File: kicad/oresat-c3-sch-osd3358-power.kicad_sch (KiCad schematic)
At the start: 52 parts, among them Q6 MMBT2907, U1 OSD3358-512M-BSM, U10 SN74LVC1G07DCK, U13 RCLAMP0504FB, U14 TLVH431

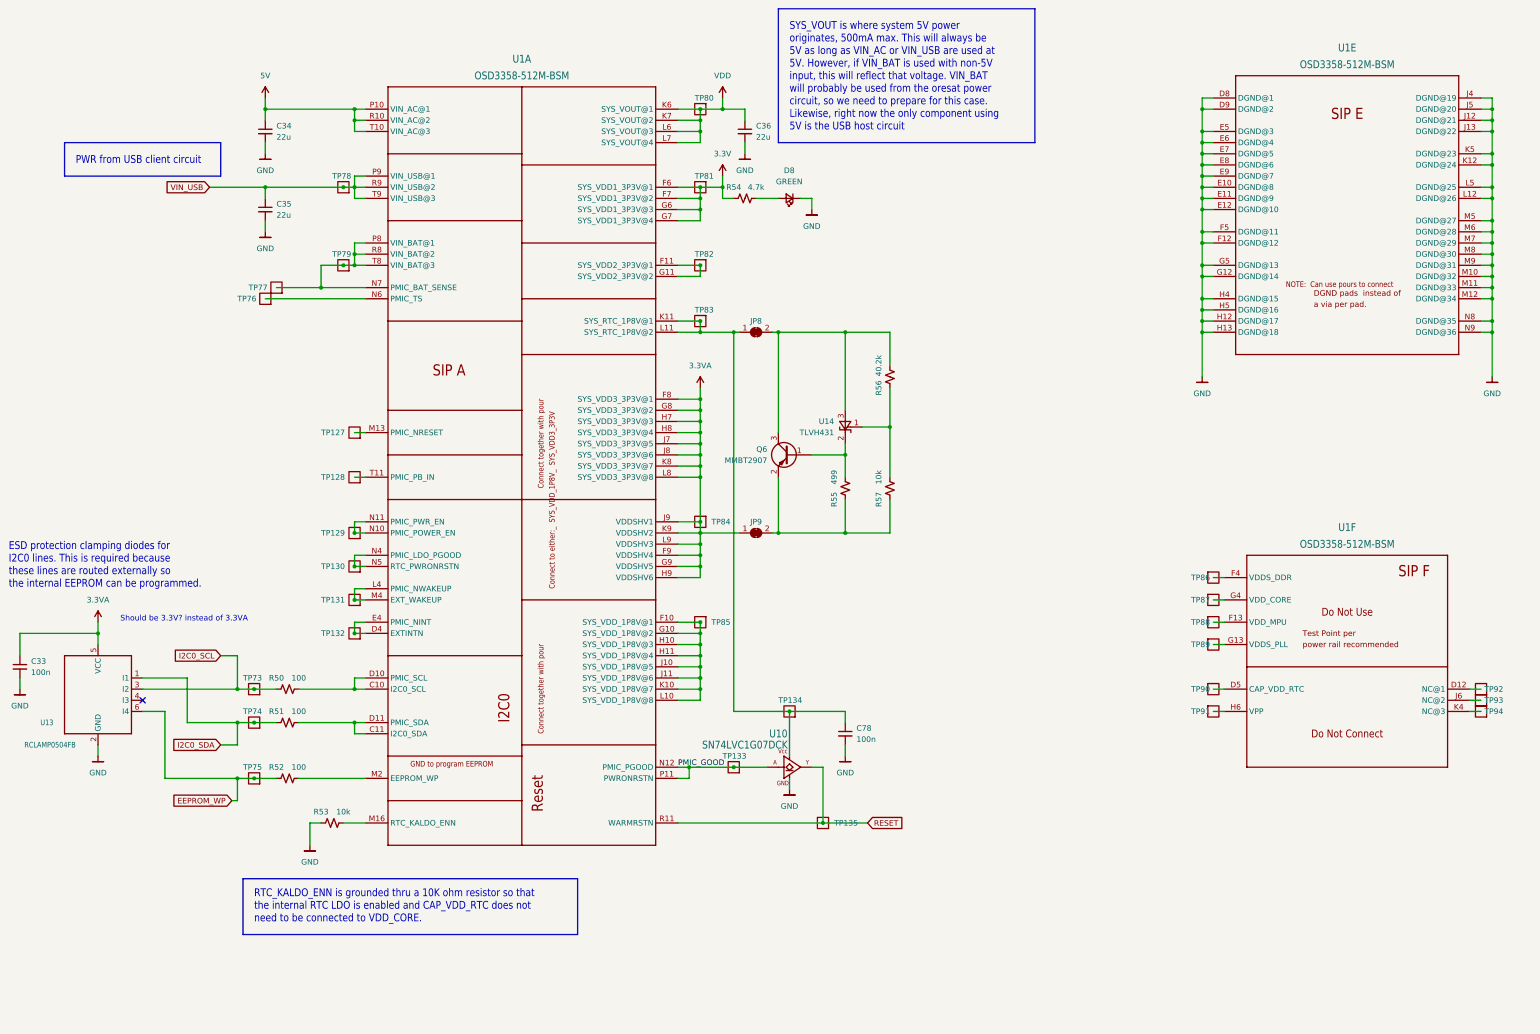
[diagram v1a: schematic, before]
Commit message: C3 v6 schematic now 80% done. OSD2258 IC has been gone over with a fine tooth comb and simplified as much as possible. OSD3358 pinout compared to RED board and PocketBeagle. What's left: lots of little issues, footprints, and then L band and UHF radio schematics need to be fixed.
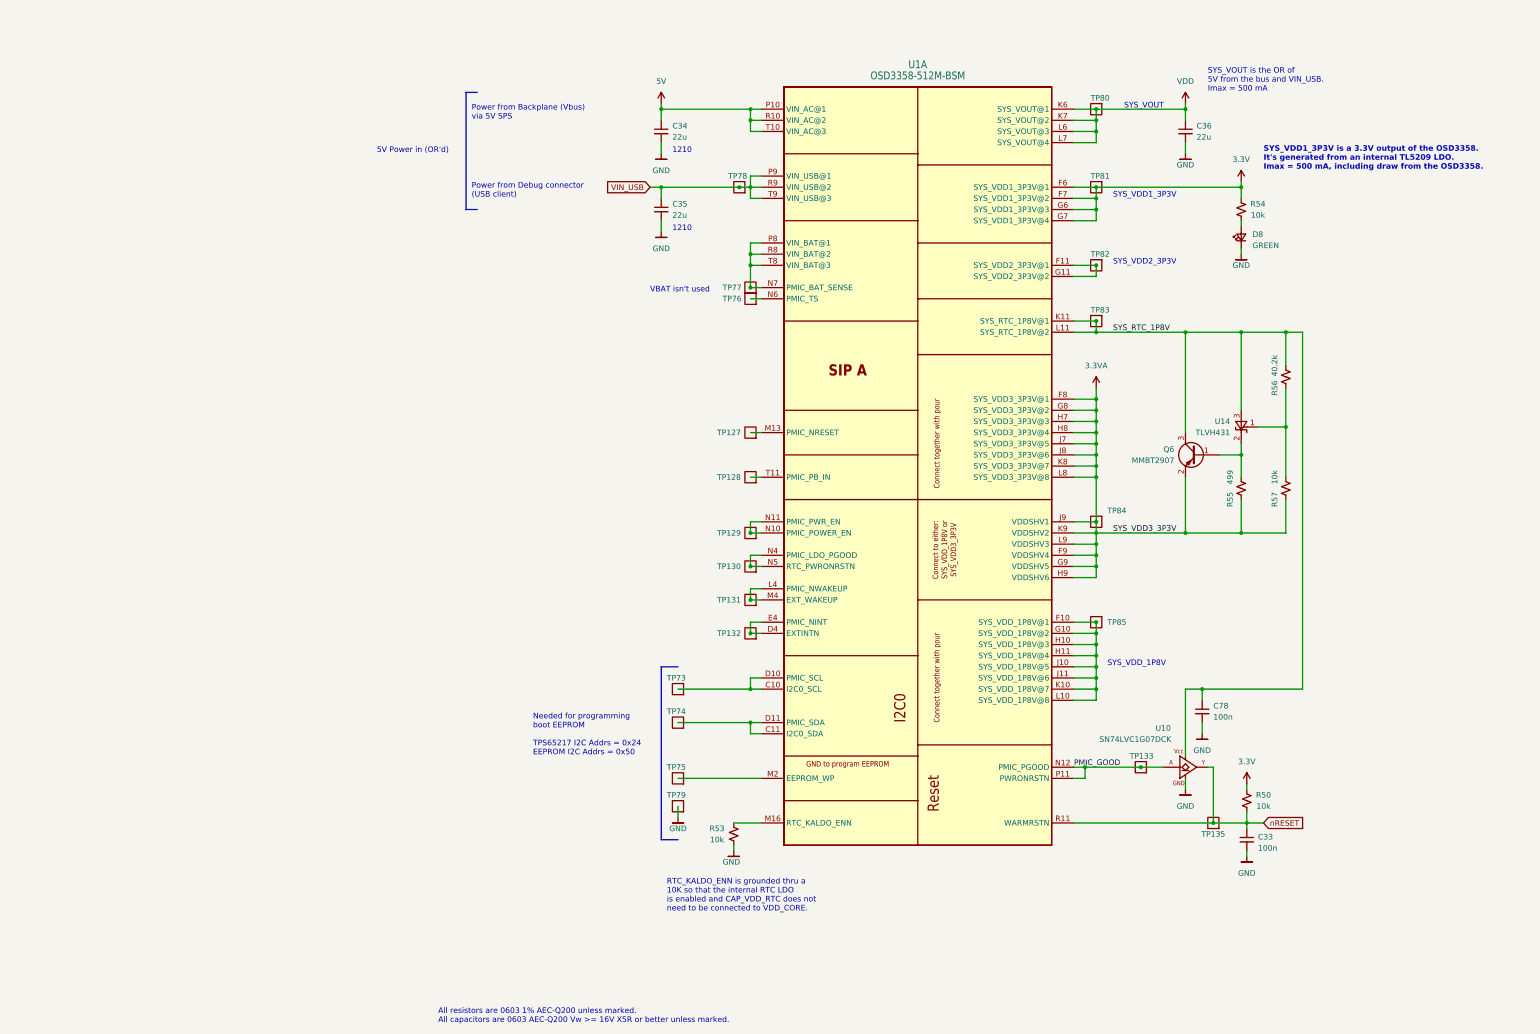
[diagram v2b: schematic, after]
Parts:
- removed JP8, JP9: SolderJumper_2_Bridged, oresat-footprints:SMT-JUMPER_2_NC_TRACE_SILK, symbol Jumper:SolderJumper_2_Bridged
- removed R51, R52: 100, Resistor_SMD:R_0603_1608Metric, symbol Device:R_Small_US
- removed TP134, TP86, TP87, TP88, TP89, TP90, TP91, TP92, TP93, TP94: Test-Point, OreSat-TestPoint:PAD.03X.04, symbol OreSat-TestPoint:Test-Point
- removed unit 6 of U1
- removed unit 5 of U1
- removed U13: RCLAMP0504FB, Package_TO_SOT_SMD:SOT-363_SC-70-6, symbol U-Semtech-RCLAMP0504FB-tvs-diodes:RCLAMP0504FB
- R50: value 100 -> 10k
- R54: value 4.7k -> 10k
- U1: symbol U-OSD3358-512M-BSM:OSD3358-512M-BSM -> oresat-ics:OSD3358-512M-BSM
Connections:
- net EEPROM_WP is gone; now on an unnamed net: TP75.1
- net I2C0_SDA is gone; now on an unnamed net: TP74.1
- net RESET is gone; now on net nRESET: TP135.1, U1.R11 (WARMRSTN), U10.4 (Y)
- net 3.3V: now also R50.2
- net 3.3VA: now also Q6.2 (E), R55.1, R57.1; no longer C33.1
- net GND: now also TP79.1
- net SYS_RTC_1P8V: now reaches C78.1, TP83.1, U1.K11 (SYS_RTC_1P8V@1), U1.L11 (SYS_RTC_1P8V@2), U10.5 (VCC)
- net SYS_RTC_1P8V: now also Q6.3 (C), R56.2, U14.3 (A)
- net at TP77.1, U1.N7 (PMIC_BAT_SENSE), U1.P8 (VIN_BAT@1)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: no longer TP79.1
- net at U1.C10 (I2C0_SCL), U1.D10 (PMIC_SCL): now also TP73.1; no longer R50.2
- net I2C0_SCL renamed nRESET
- net nRESET: now also C33.1; no longer TP73.1
- no-connect marks 1 -> 0
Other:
- note added: "1210"
- note added: "5V Power in (OR'd)"
- note added: "All resistors are 0603 1% AEC-Q200 unless marked. All capacitors are 0603 AEC-Q200 Vw >= 16V X5R or better unless marked."
- note added: "Needed for programming boot EEPROM TPS65217 I2C Addrs = 0x24 EEPROM I2C Addrs = 0x50"
- note added: "Power from Backplane (Vbus) via 5V SPS"
- note added: "Power from Debug connector (USB client)"
- note added: "RTC_KALDO_ENN is grounded thru a 10K so that the internal RTC LDO is enabled and CAP_VDD_RTC does not need to be connected to VDD_CORE."
- note added: "SYS_VDD1_3P3V"
- note added: "SYS_VDD1_3P3V is a 3.3V output of the OSD3358. It's generated from an internal TL5209 LDO. Imax = 500 mA, including draw from the OSD3358."
- note added: "SYS_VDD2_3P3V"
- note added: "SYS_VDD_1P8V"
- note added: "SYS_VOUT"
- note added: "SYS_VOUT is the OR of 5V from the bus and VIN_USB. Imax = 500 mA"
- note added: "VBAT isn't used"
- note removed: "ESD protection clamping diodes for I2C0 lines. This is required because these lines are routed externally so the internal EEPROM can be programmed."
- note removed: "PWR from USB client circuit"
- note removed: "RTC_KALDO_ENN is grounded thru a 10K ohm resistor so that the internal RTC LDO is enabled and CAP_VDD_RTC does not need to be connected to VDD_CORE."
- note removed: "SYS_VOUT is where system 5V power originates, 500mA max. This will always be 5V as long as VIN_AC or VIN_USB are used at 5V. However, if VIN_BAT is used with non-5V input, this will reflect that voltage. VIN_BAT will probably be used from the oresat power circuit, so we need to prepare for this case. Likewise, right now the only component using 5V is the USB host circuit"
- note removed: "Should be 3.3V? instead of 3.3VA"
- title: (none) -> OreSat C3: OSD3358: SIP A
- moved on the sheet: C34, C35, C36, C78, D8, Q6, R53, R54, R55, R56, R57, TP127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

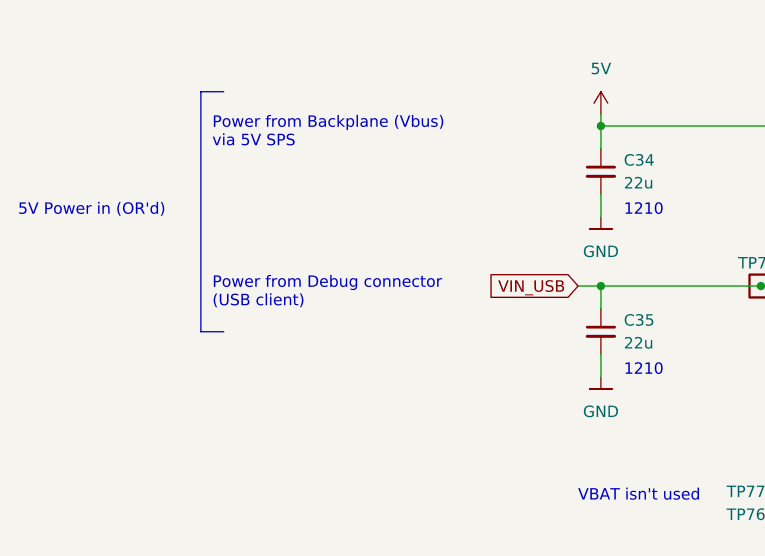
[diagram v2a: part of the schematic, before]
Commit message: Finished UHF radio schematic. Added sheet numbers to external labels. Still to do: L band radio, hooking up GPIO to the OSD3358, and test points.
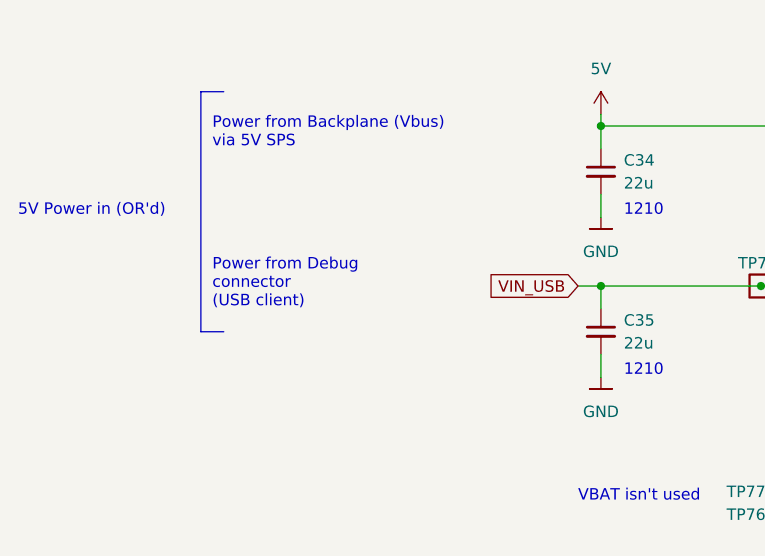
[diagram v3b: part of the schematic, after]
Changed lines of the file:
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@@
     (effects (font (size 1.27 1.27) (thickness 0.254) bold) (justify left bottom))
   )
-  (text "Power from Debug connector\n(USB client)" (at 123.19 73.66 0)
+  (text "Power from Debug \nconnector\n(USB client)" (at 123.19 73.66 0)
     (effects (font (size 1.27 1.27)) (justify left bottom))
   )
@@
     (effects (font (size 1.27 1.27)) (justify right))
     (property "Intersheetrefs" "${INTERSHEET_REFS}" (at 153.6155 71.0406 0)
-      (effects (font (size 1.27 1.27)) (justify right) hide)
+      (effects (font (size 1.27 1.27)) (justify right))
     )
   )
@@
     (effects (font (size 1.27 1.27)) (justify left))
     (property "Intersheetrefs" "${INTERSHEET_REFS}" (at 313.3299 215.9 0)
-      (effects (font (size 1.27 1.27)) (justify left) hide)
+      (effects (font (size 1.27 1.27)) (justify left))
     )
   )

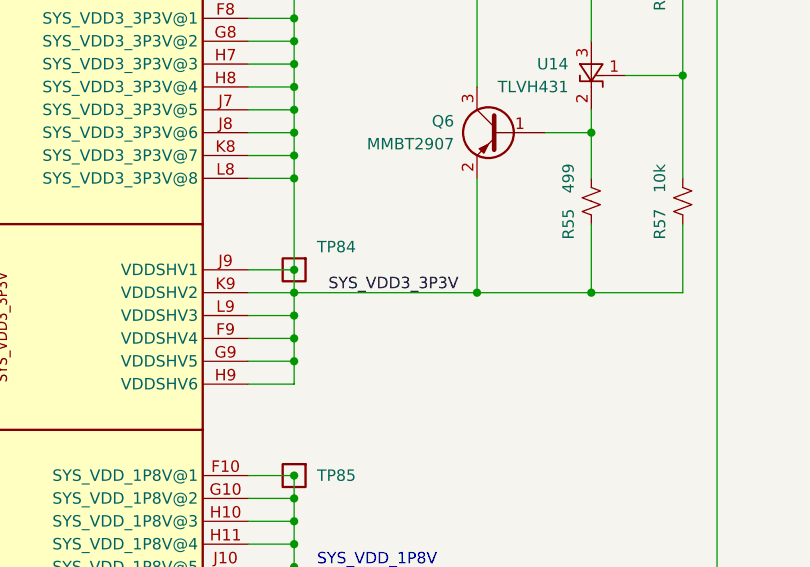
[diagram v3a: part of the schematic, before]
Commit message: First round of ERC fixes.
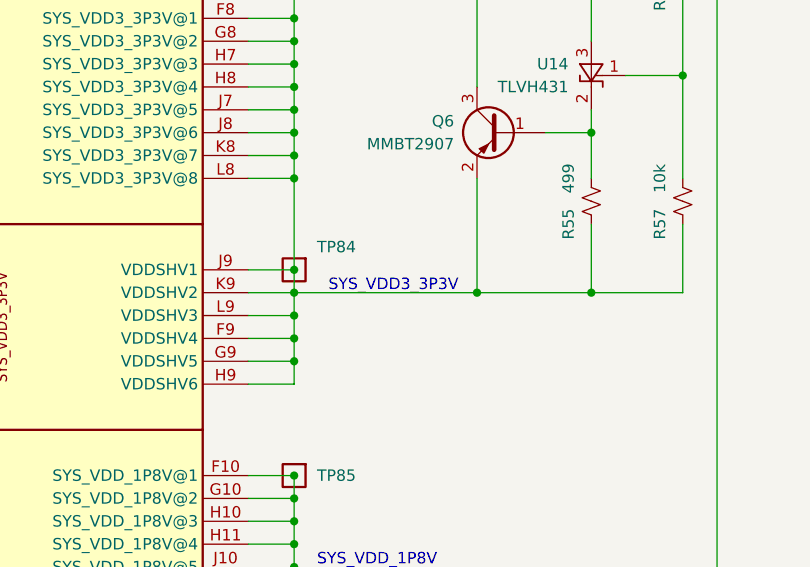
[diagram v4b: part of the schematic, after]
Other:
- note added: "SYS_VDD3_3P3V"
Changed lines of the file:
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@@
+    (effects (font (size 1.27 1.27)) (justify left bottom))
+  )
+  (text "SYS_VDD3_3P3V" (at 269.24 149.86 0)
     (effects (font (size 1.27 1.27)) (justify left bottom))
   )
@@
     (effects (font (size 1.27 1.27)) (justify left bottom))
   )
-  (label "SYS_VDD3_3P3V" (at 269.24 149.86 0) (fields_autoplaced)
-    (effects (font (size 1.27 1.27)) (justify left bottom))
-  )
